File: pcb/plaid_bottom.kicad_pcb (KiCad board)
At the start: 2 copper layers, 228 x 98 mm, 12 parts

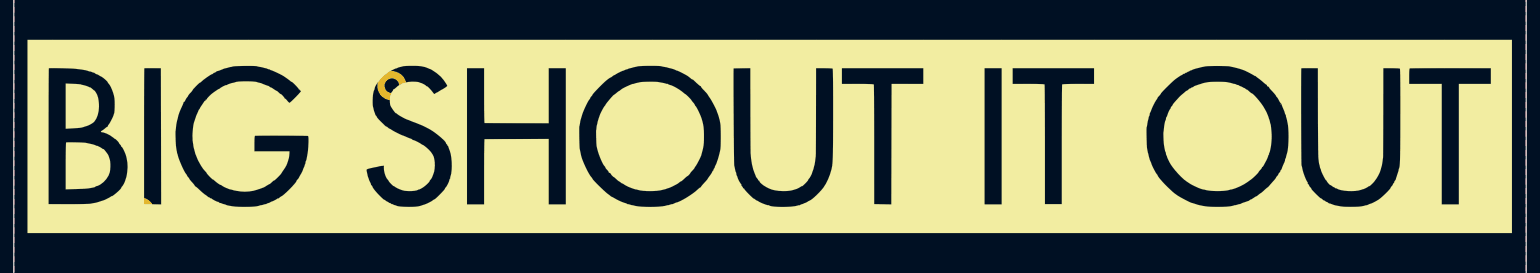
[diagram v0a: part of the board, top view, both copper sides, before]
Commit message: remove silk screen
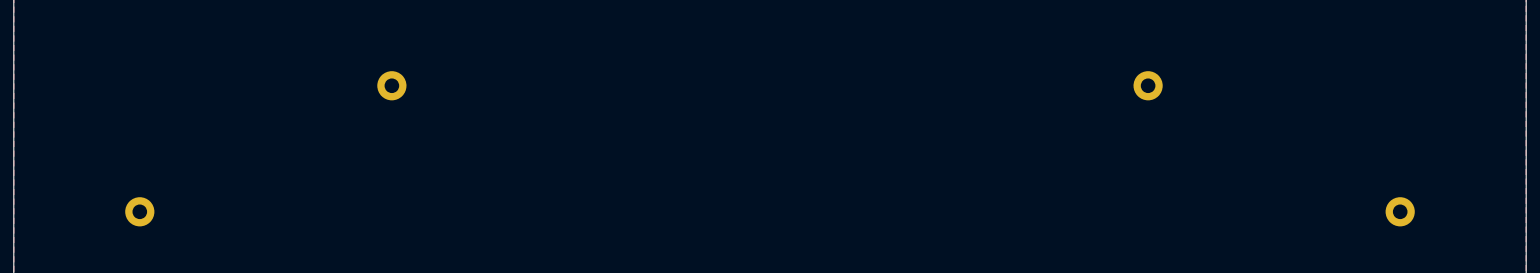
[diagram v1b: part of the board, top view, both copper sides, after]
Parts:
- removed G***: LOGO, plaid_silk:plaid_bottomA
- removed G***: LOGO, plaid_silk:plaid_bottomB
